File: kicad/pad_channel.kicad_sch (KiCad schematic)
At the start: 14 parts, among them J501 JST_B11P_SHF_1AA, Q501 AO3400A, U501 SRV05-4

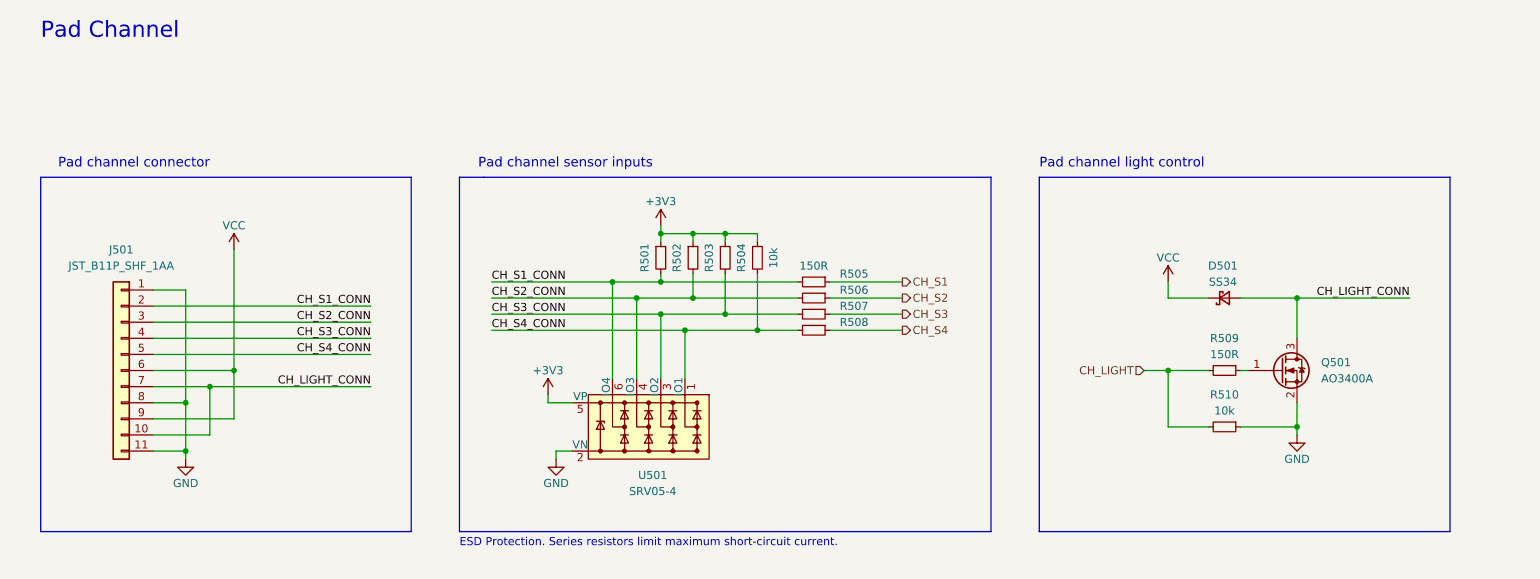
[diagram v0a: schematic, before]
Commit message: Add PTC fuses on lights drivers and before switching regulator.
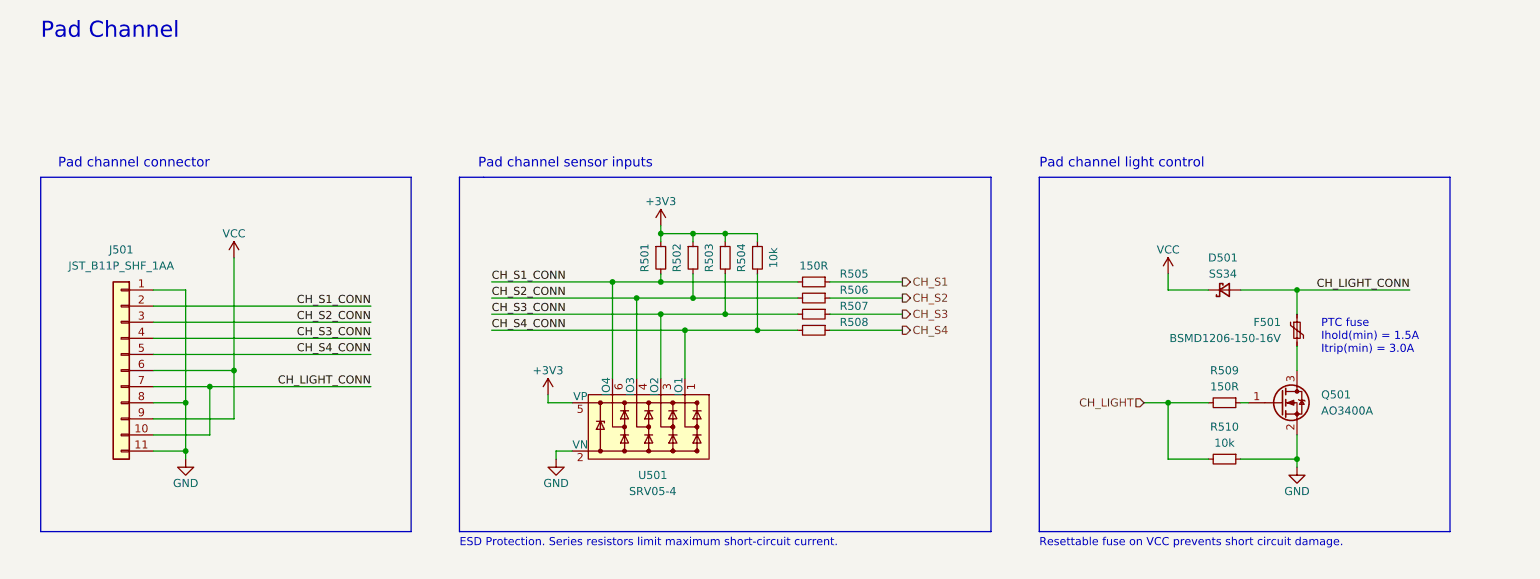
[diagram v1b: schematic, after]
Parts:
- added F501: BSMD1206-150-16V, Fuse:Fuse_1206_3216Metric_Pad1.42x1.75mm_HandSolder, symbol Device:Polyfuse_Small
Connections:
- net CH_LIGHT_CONN: now also F501.1; no longer Q501.3 (D)
- new net: F501.2, Q501.3 (D)
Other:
- note added: "PTC fuse Ihold(min) = 1.5A Itrip(min) = 3.0A"
- note added: "Resettable fuse on VCC prevents short circuit damage."
- moved on the sheet: D501, Q501, R509, R510

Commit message: Update to v1.1.0
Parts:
- D501: JLCPCB Part # (none) -> C8678
- F501: JLCPCB Part # (none) -> C883133
- Q501: JLCPCB Part # (none) -> C20917
- R501, R502, R503, R504, R510: JLCPCB Part # (none) -> C25804
- R505, R506, R507, R508, R509: JLCPCB Part # (none) -> C22808
- U501: JLCPCB Part # (none) -> C85364
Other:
- company: BlueDot, Vincenzo Fortunato -> BlueDot Arcade, Vincenzo Fortunato
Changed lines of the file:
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@@
   (title_block
     (title "BD845-PWB SCH")
-    (date "2022-11-27")
-    (rev "1.0.0")
-    (company "BlueDot, Vincenzo Fortunato")
+    (date "2023-06-14")
+    (rev "1.1.0")
+    (company "BlueDot Arcade, Vincenzo Fortunato")
+    (comment 1 "bluedotarcade.com")
   )
   (junction (at 123.19 90.17) (diameter 0) (color 0 0 0 0)
@@
       (effects (font (size 1.27 1.27)) hide)
     )
+    (property "JLCPCB Part #" "C25804" (at 219.71 118.11 0)
+      (effects (font (size 1.27 1.27)) hide)
+    )
     (pin "1")
     (pin "2")
@@
     )
     (property "Datasheet" "http://www.onsemi.com/pub/Collateral/SRV05-4-D.PDF" (at 124.46 92.71 0)
+      (effects (font (size 1.27 1.27)) hide)
+    )
+    (property "JLCPCB Part #" "C85364" (at 129.54 113.03 0)
       (effects (font (size 1.27 1.27)) hide)
     )
@@
       (effects (font (size 1.27 1.27)) hide)
     )
+    (property "JLCPCB Part #" "C25804" (at 135.89 86.36 0)
+      (effects (font (size 1.27 1.27)) hide)
+    )
     (pin "1")
     (pin "2")
@@
     )
     (property "Datasheet" "~" (at 45.72 104.14 0)
+      (effects (font (size 1.27 1.27)) hide)
+    )
+    (property "JLCPCB Part #" "" (at 45.72 104.14 0)
       (effects (font (size 1.27 1.27)) hide)
     )
@@
       (effects (font (size 1.27 1.27)) hide)
     )
+    (property "JLCPCB Part #" "C25804" (at 130.81 86.36 0)
+      (effects (font (size 1.27 1.27)) hide)
+    )
     (pin "1")
     (pin "2")
@@
       (effects (font (size 1.27 1.27)) (justify left) hide)
     )
+    (property "JLCPCB Part #" "C20917" (at 228.6 109.22 0)
+      (effects (font (size 1.27 1.27)) hide)
+    )
     (pin "1")
     (pin "2")
@@
     )
     (property "Datasheet" "~" (at 154.94 90.17 0)
+      (effects (font (size 1.27 1.27)) hide)
+    )
+    (property "JLCPCB Part #" "C22808" (at 154.94 90.17 0)
       (effects (font (size 1.27 1.27)) hide)
     )
@@
       (effects (font (size 1.27 1.27)) hide)
     )
+    (property "JLCPCB Part #" "C25804" (at 140.97 86.36 0)
+      (effects (font (size 1.27 1.27)) hide)
+    )
     (pin "1")
     (pin "2")
@@
     )
     (property "Datasheet" "~" (at 231.14 97.79 0)
+      (effects (font (size 1.27 1.27)) hide)
+    )
+    (property "JLCPCB Part #" "C883133" (at 231.14 97.79 0)
       (effects (font (size 1.27 1.27)) hide)
     )
@@
       (effects (font (size 1.27 1.27)) hide)
     )
+    (property "JLCPCB Part #" "C22808" (at 219.71 109.22 0)
+      (effects (font (size 1.27 1.27)) hide)
+    )
     (pin "1")
     (pin "2")
@@
       (effects (font (size 1.27 1.27)) hide)
     )
+    (property "JLCPCB Part #" "C22808" (at 154.94 92.71 0)
+      (effects (font (size 1.27 1.27)) hide)
+    )
     (pin "1")
     (pin "2")
@@
       (effects (font (size 1.27 1.27)) hide)
     )
+    (property "JLCPCB Part #" "C22808" (at 154.94 97.79 0)
+      (effects (font (size 1.27 1.27)) hide)
+    )
     (pin "1")
     (pin "2")
@@
       (effects (font (size 1.27 1.27)) hide)
     )
+    (property "JLCPCB Part #" "C22808" (at 154.94 95.25 0)
+      (effects (font (size 1.27 1.27)) hide)
+    )
     (pin "1")
     (pin "2")
@@
     )
     (property "Datasheet" "~" (at 219.71 91.44 90)
+      (effects (font (size 1.27 1.27)) hide)
+    )
+    (property "JLCPCB Part #" "C8678" (at 219.71 91.44 0)
       (effects (font (size 1.27 1.27)) hide)
     )
@@
       (effects (font (size 1.27 1.27)) hide)
     )
+    (property "JLCPCB Part #" "C25804" (at 146.05 86.36 0)
+      (effects (font (size 1.27 1.27)) hide)
+    )

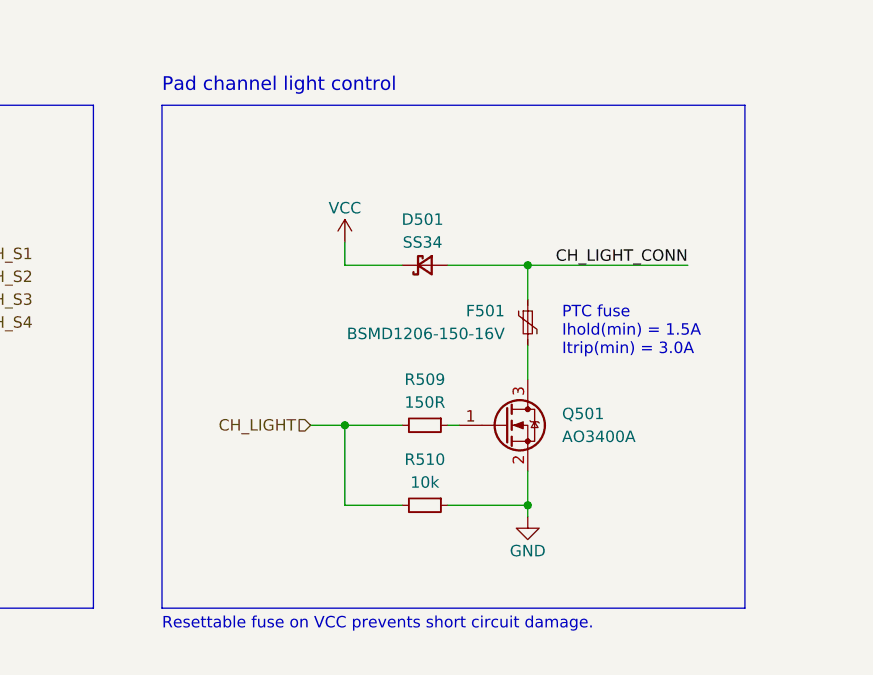
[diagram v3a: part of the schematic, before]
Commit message: Change light driver to a self-protected mosfet. Remove unnecessary fuses. Change 74HC595 to low input voltage equivalent. Change LED resistors to 1k. Power lights shift register with +5V.
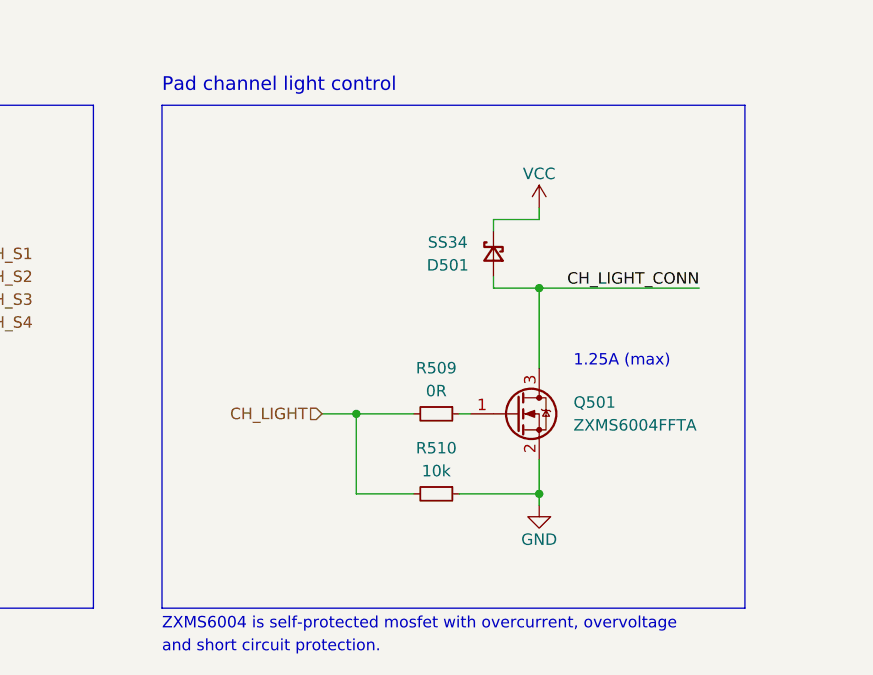
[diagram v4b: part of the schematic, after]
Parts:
- removed F501: BSMD1206-150-16V, Fuse:Fuse_1206_3216Metric_Pad1.42x1.75mm_HandSolder, symbol Device:Polyfuse_Small
- Q501: value AO3400A -> ZXMS6004FFTA; footprint Package_TO_SOT_SMD:SOT-23 -> ProjectLibrary:SOT23F; symbol Transistor_FET:AO3400A -> ProjectLibrary:ZXMS6004FFTA; JLCPCB Part # C20917 -> C95063
- R509: value 150R -> 0R; JLCPCB Part # C22808 -> C21189
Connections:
- net CH_LIGHT_CONN: now also Q501.3 (D)
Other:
- note added: "1.25A (max)"
- note added: "ZXMS6004 is self-protected mosfet with overcurrent, overvoltage"
- note added: "and short circuit protection."
- note removed: "PTC fuse Ihold(min) = 1.5A Itrip(min) = 3.0A"
- note removed: "Resettable fuse on VCC prevents short circuit damage."
- moved on the sheet: D501, Q501, R509, R510
